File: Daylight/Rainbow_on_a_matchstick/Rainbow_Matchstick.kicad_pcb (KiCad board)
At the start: 2 copper layers, 158 x 11 mm, 24 parts, among them J1 Conn_01x03_Male, J2 Conn_01x01_Male, J3 Conn_01x01_Male

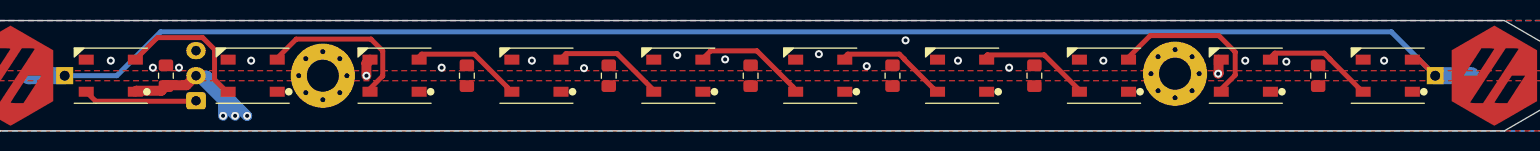
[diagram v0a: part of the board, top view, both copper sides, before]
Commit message: Daylight | Add output connectors to the RGB sticks
Provided pick and place files for all varieties as well.
Created individual README.md files with BOM and changelog.
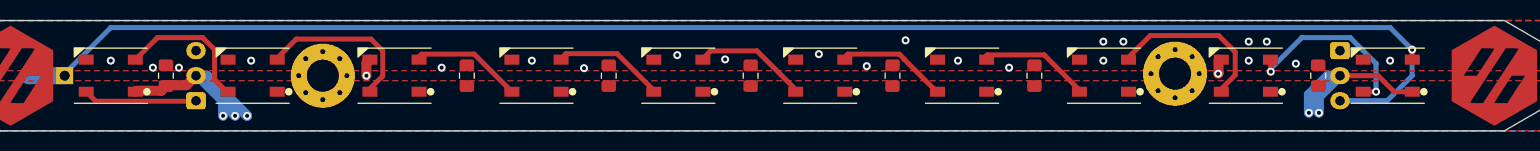
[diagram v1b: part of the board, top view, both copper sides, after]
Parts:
- J2: value Conn_01x01_Male -> Conn_01x03_Male; footprint Daylight:PinHeader-1-with-SMDpad -> Daylight:JST_XH_S3B-XH-A-1_1x03_P2.50mm_Horizontal
- moved J2 9.82 mm to (150.6, 30.5), turned to -90 degrees
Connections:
- J2 pad 1: DOUT -> GND
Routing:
- net +5V: track 23.7 -> 41.8 mm, vias 3 -> 5
- net Net-(D10-Pad4): track 11.3 -> 18.5 mm, vias 0 -> 2
- net DOUT: track 143.5 -> 149.2 mm, vias 0 -> 1
- net GND: vias 20 -> 24
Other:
- board text added: "GND 5V DOUT"
- board text added: "Rainbow Matchstick v1.1 by Blamm"
- board text removed: "Rainbow Matchstick v1.0 by Blamm"
